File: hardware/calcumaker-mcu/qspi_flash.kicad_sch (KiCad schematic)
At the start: 3 parts, among them U7 W25Q32JVSSIQ

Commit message: Checkpoint
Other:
- note added: "QSPI FLASH - U7 W25Q32JVSSIQ (LCSC C179173) 4MB (32Mbit) quad-SPI NOR, SOIC-8, 2.7-3.6V, on the STM32U575 OCTOSPI1. PIN SIGNAL 1 CS# <- NCS PA4 AF3 p20 (+R9 10k) 6 CLK <- CLK PB10 AF10 p29 5 IO0 / DI <-> IO0 PB1 AF10 p27 2 IO1 / DO <-> IO1 PB0 AF10 p26 3 IO2 / WP# <-> IO2 PA7 AF10 p23 7 IO3 / HOLD# <-> IO3 PA6 AF10 p22 8 VCC = +3V3 (C26 100nF at pin 8) 4 GND OCTOSPI on U5 goes through the OCTOSPI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"
- note removed: "QSPI FLASH - U7 W25Q32JVSSIQ (LCSC C179173) 4MB (32Mbit) quad-SPI NOR, SOIC-8, 2.7-3.6V, on the STM32U575 OCTOSPI1. PIN SIGNAL U575 PIN AF PKG 1 CS# <- NCS PA4 AF3 20 (+R9 10k) 6 CLK <- CLK PB10 AF10 29 5 IO0 / DI <-> IO0 PB1 AF10 27 2 IO1 / DO <-> IO1 PB0 AF10 26 3 IO2 / WP# <-> IO2 PA7 AF10 23 7 IO3 / HOLD# <-> IO3 PA6 AF10 22 8 VCC = +3V3 (C26 100nF at pin 8) 4 GND OCTOSPI on U5 goes through t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"

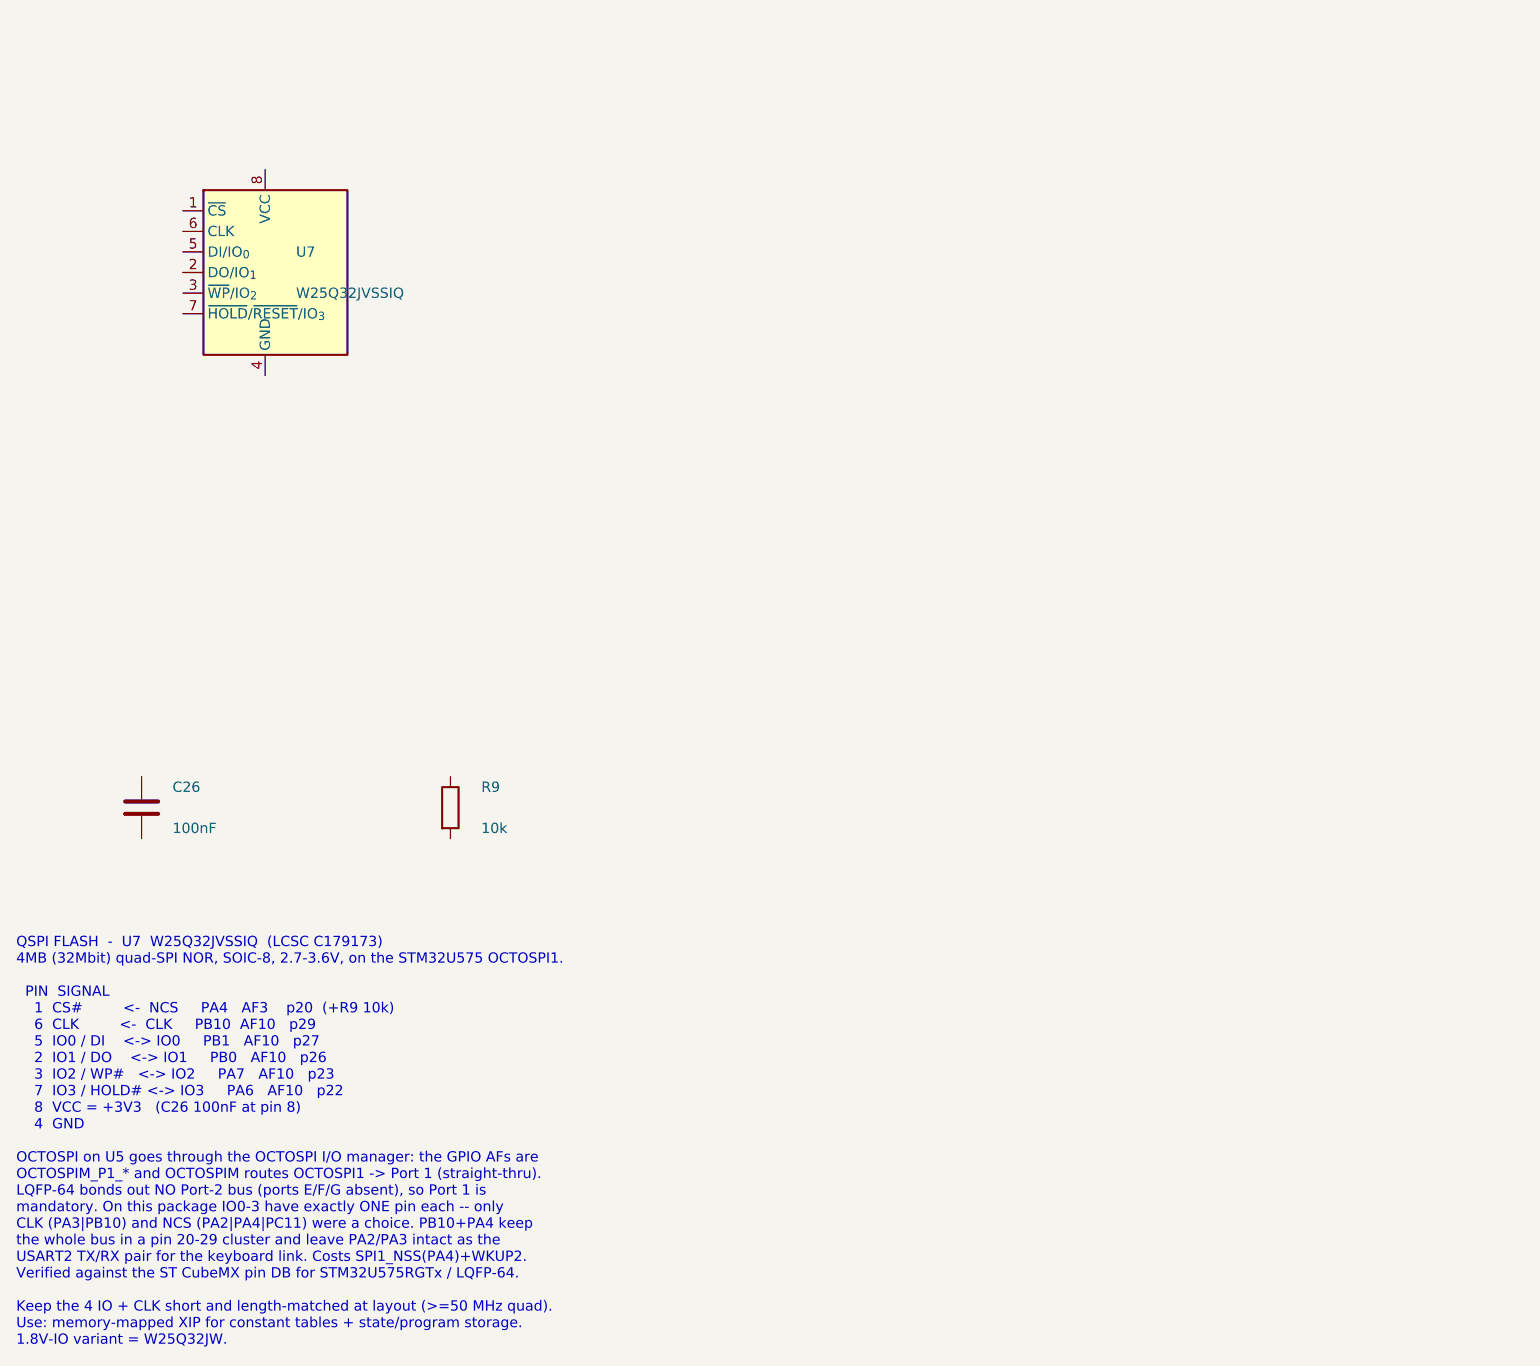
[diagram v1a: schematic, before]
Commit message: Wire mainboard and keypad schematics and verify expanded nets
Connect hierarchical interfaces, power/control circuits, debug links, matrix and RGB chains. Correct MCU package pins, diode polarity and power configuration; add bypass components and repeatable KiCad netlist/ERC checks. Document pin maps and remaining physical validation.
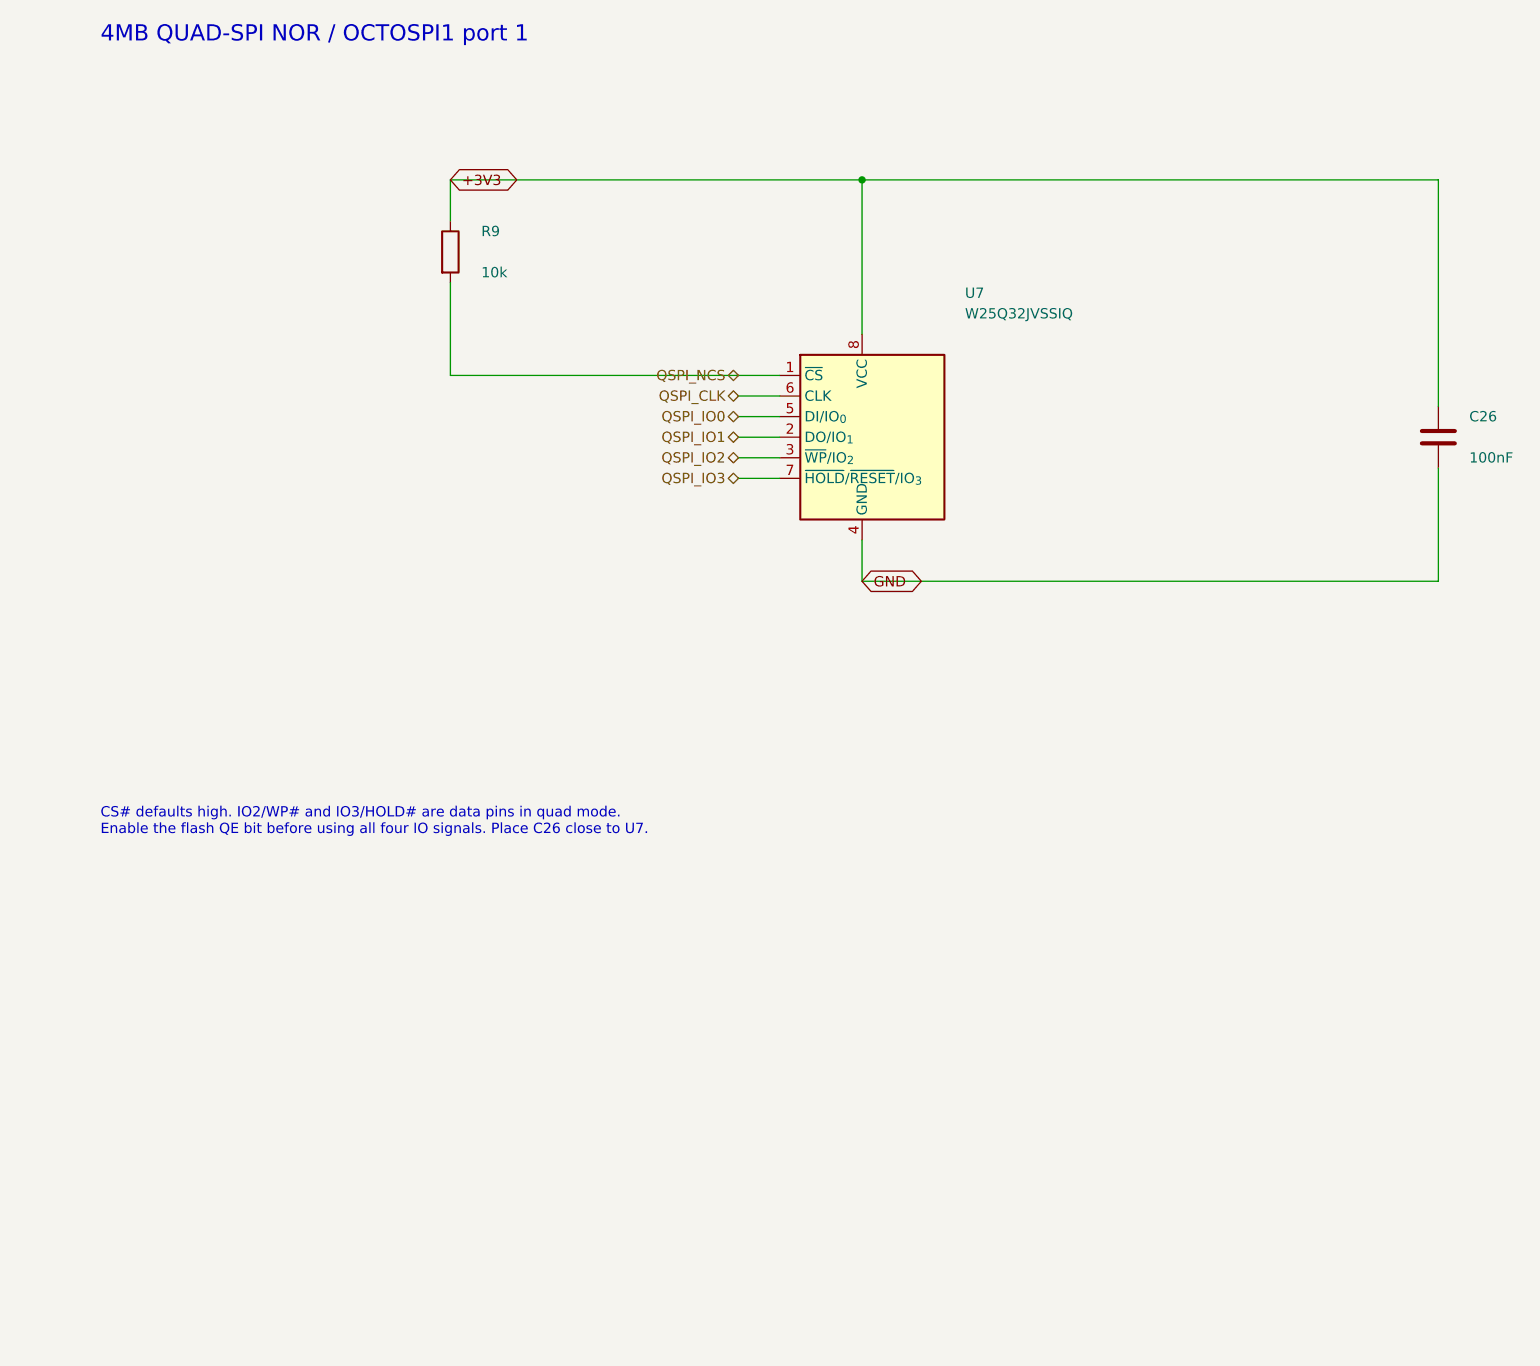
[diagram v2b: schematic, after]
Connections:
- net +3V3: now reaches C26.1
- net +3V3: now also R9.1, U7.8 (VCC)
- net GND: now reaches C26.2
- net GND: now also U7.4 (GND)
- net QSPI_NCS: now reaches U7.1 (~{CS})
- net QSPI_NCS: now also R9.2
- net QSPI_IO1: now reaches U7.2 (DO/IO_{1})
- net QSPI_IO2: now reaches U7.3 (~{WP}/IO_{2})
- net QSPI_IO0: now reaches U7.5 (DI/IO_{0})
- net QSPI_CLK: now reaches U7.6 (CLK)
- net QSPI_IO3: now reaches U7.7 (~{HOLD}/~{RESET}/IO_{3})
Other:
- note added: "4MB QUAD-SPI NOR / OCTOSPI1 port 1"
- note added: "CS# defaults high. IO2/WP# and IO3/HOLD# are data pins in quad mode. Enable the flash QE bit before using all four IO signals. Place C26 close to U7."
- note removed: "QSPI FLASH - U7 W25Q32JVSSIQ (LCSC C179173) 4MB (32Mbit) quad-SPI NOR, SOIC-8, 2.7-3.6V, on the STM32U575 OCTOSPI1. PIN SIGNAL 1 CS# <- NCS PA4 AF3 p20 (+R9 10k) 6 CLK <- CLK PB10 AF10 p29 5 IO0 / DI <-> IO0 PB1 AF10 p27 2 IO1 / DO <-> IO1 PB0 AF10 p26 3 IO2 / WP# <-> IO2 PA7 AF10 p23 7 IO3 / HOLD# <-> IO3 PA6 AF10 p22 8 VCC = +3V3 (C26 100nF at pin 8) 4 GND OCTOSPI on U5 goes through the OCTOSPI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"
- title: Calcumaker 16 — MCU — 4MB quad-SPI NOR flash (OCTOSPI1) -> Calcumaker 16 / mcu / qspi flash
- moved on the sheet: C26, R9, U7
